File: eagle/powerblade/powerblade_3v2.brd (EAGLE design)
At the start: 25.4 x 25.4 mm, 80 parts, among them J1 JTAG_14PIN_IDC-ND, J2 AC_INF3, J4 TC2030-JLINK-NL, Q1 NTS4173, Q4 2SK1829, U1 TPS62122, U2 MCP6V3, U3 MSP430FR5738, U4 NRF51822QF, U6 MAX9910, U7 OPA2369, X1 16MHz, X3 32.768kHz, Y1 UREACH_XTEND

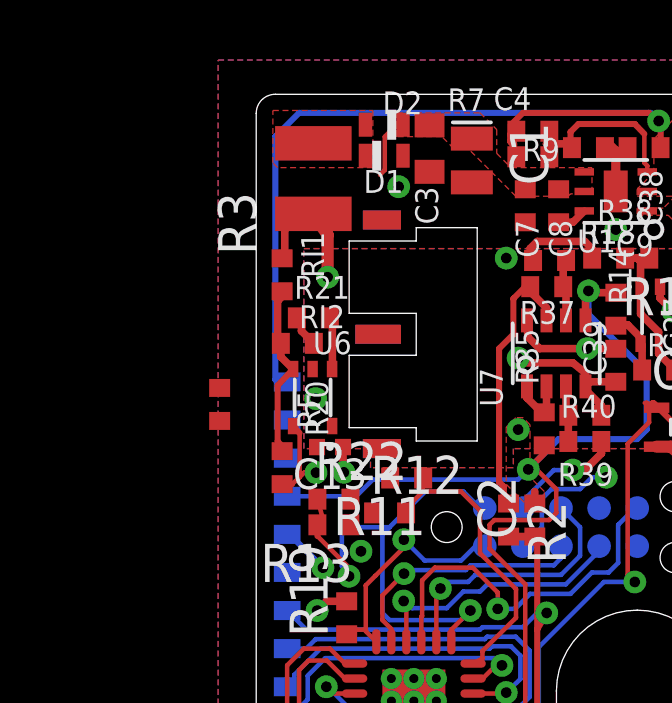
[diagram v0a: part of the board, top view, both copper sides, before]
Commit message: disconnected all but A.4 in F3
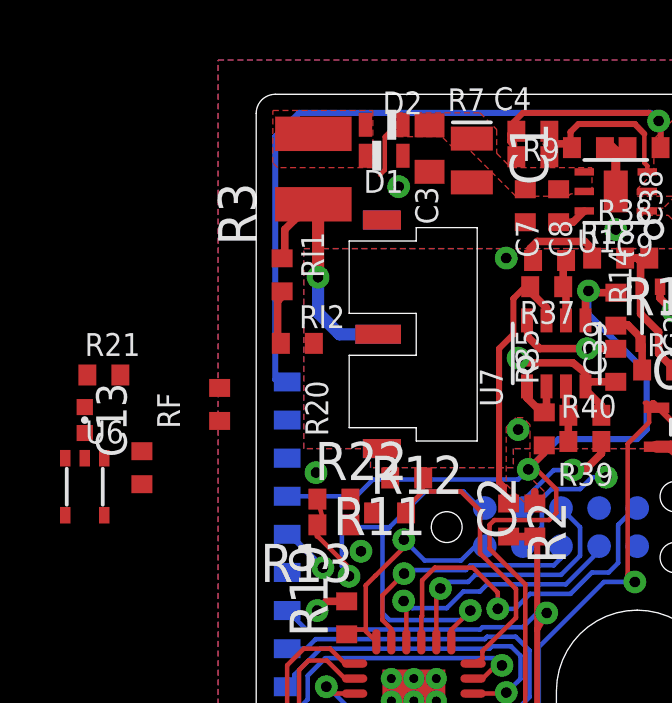
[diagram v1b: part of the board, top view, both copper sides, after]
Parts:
- moved C13 8.23 mm to (-18.4, -2.86), turned to 270 degrees
- moved U6 8.16 mm to (-18.4, -5.08)
- moved R21 7.24 mm to (-17.8, -1.36)
- moved RF 4.67 mm to (-16.5, -4.45)
- moved R3 0.32 mm to (-10.8, 5.51)
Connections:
- net VTEST: no longer J2.PA.1, J2.PA.2, J2.PA.3, J2.PA.5, J2.PA.6
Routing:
- net N$41: track 5.87 -> 1.84 mm
- net VTEST: track 4.37 -> 8.25 mm
- net V_SENSE: track 26.6 -> 23.5 mm
- net N$40: track 1.75 -> 0.00 mm
- net GND3: track 11.5 -> 10.4 mm, vias 7 -> 6
- net +3V3: track 19.3 -> 18.5 mm, vias 10 -> 9

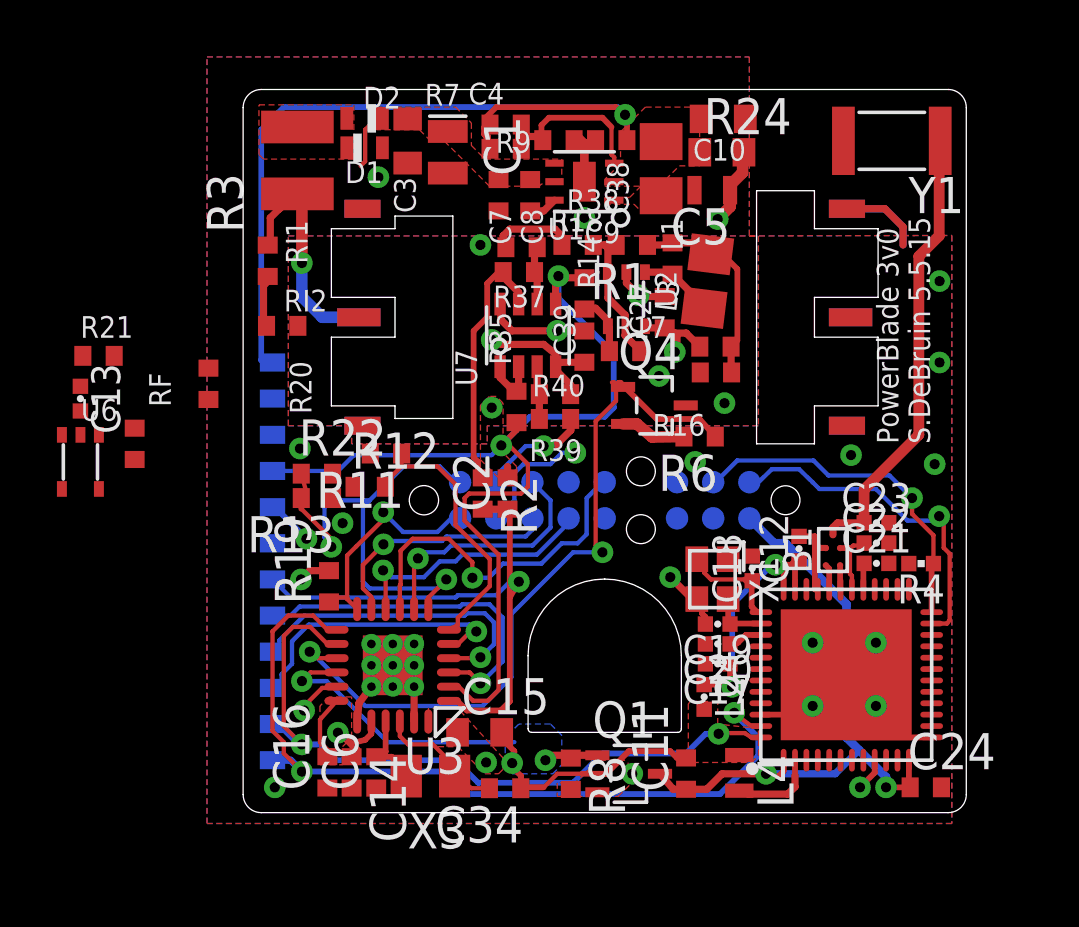
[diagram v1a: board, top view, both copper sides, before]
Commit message: more routing on powerblade and moved Phase contact to top (position 3)
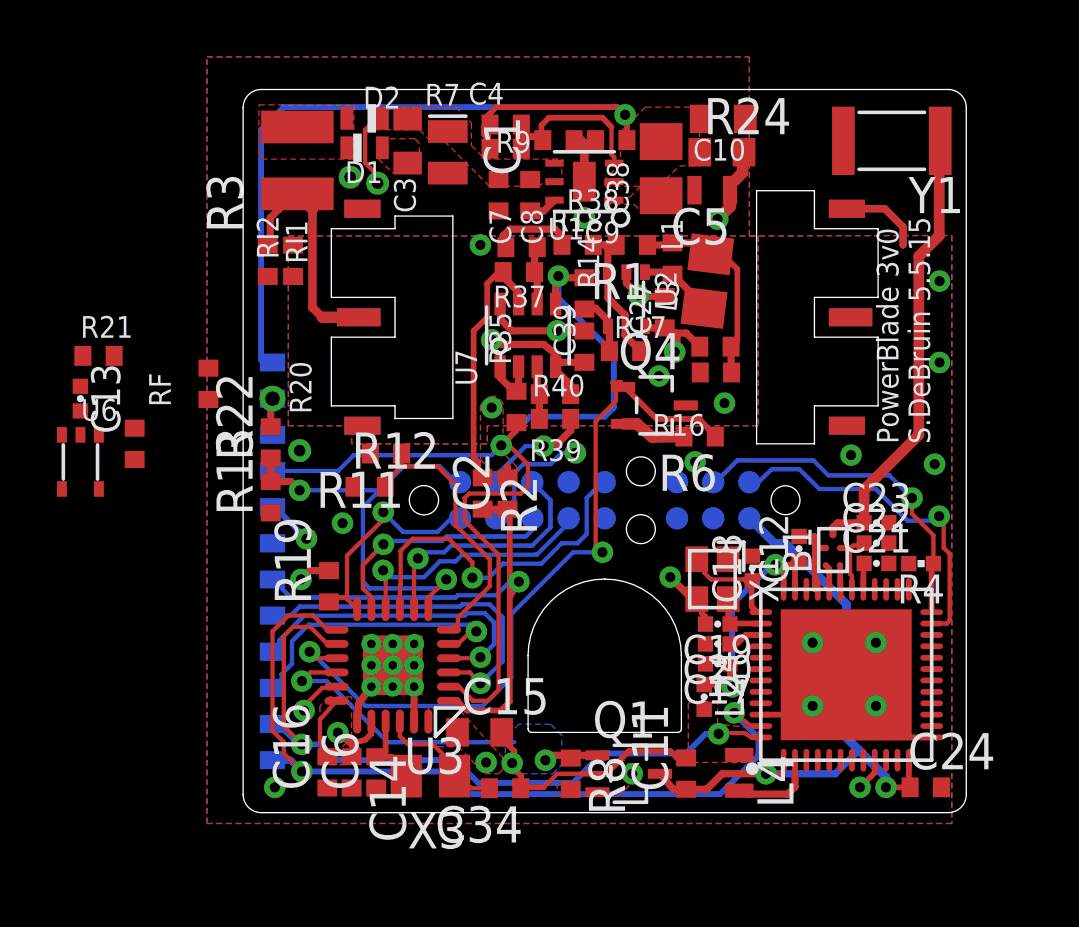
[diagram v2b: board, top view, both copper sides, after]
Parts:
- moved RI2 2.32 mm to (-10.9, 1.98), turned to 270 degrees
- moved R22 1.96 mm to (-11.7, -4.39), turned to 90 degrees
- moved R13 1.62 mm to (-11.7, -6.32), turned to 90 degrees
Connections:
- net VTEST: now also J2.PA.3; no longer J2.PA.4
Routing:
- net V_SENSE: track 23.5 -> 10.2 mm, vias 2 -> 1
- net N$41: track 1.84 -> 0.00 mm
- net TDO: track 17.7 -> 16.1 mm
- net VCC: track 2.38 -> 3.10 mm, vias 0 -> 2
- net ZC: track 0.66 -> 1.01 mm, vias 0 -> 2
- net VTEST: vias 1 -> 0
- net GND: vias 16 -> 15

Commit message: switched pins for vfilt and isense
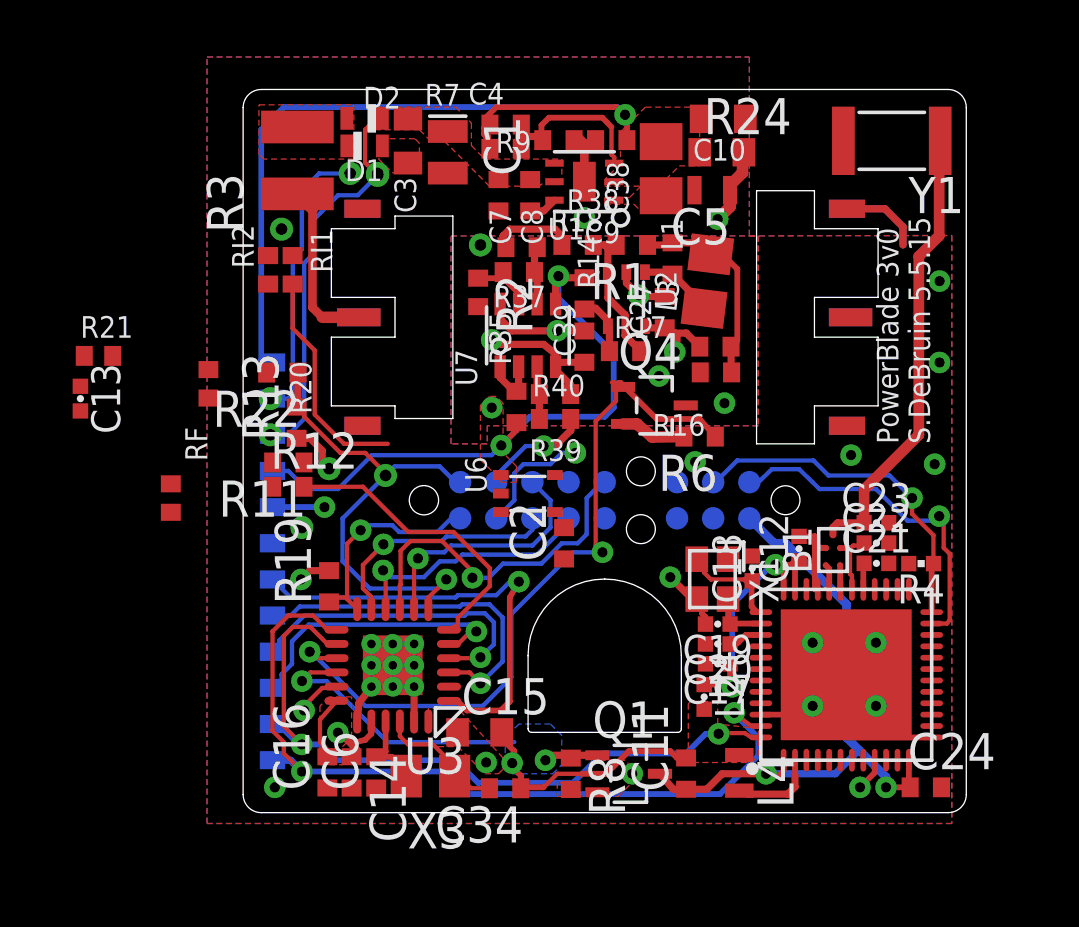
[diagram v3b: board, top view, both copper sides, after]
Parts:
- R2, R20, R21, RF, RI1, RI2: device rcl:R0402_SM -> rcl:R0402
- moved U6 15.8 mm to (-2.70, -6.19), turned to 0 degrees
- moved R2 7.07 mm to (-4.45, 0.87)
- moved R11 3.44 mm to (-11.1, -5.10)
- moved R12 2.86 mm to (-11.1, -5.95)
- moved R13 2.77 mm to (-10.8, -3.70)
- moved C2 2.64 mm to (-1.43, -7.94)
- moved R22 2.49 mm to (-11.3, -1.94), turned to 180 degrees
- moved RF 2.29 mm to (-15.2, -6.35)
- moved RI1 0.93 mm to (-11.0, 1.67)
- moved RI2 0.93 mm to (-11.8, 1.67)
- moved D1 0.07 mm to (-8.43, 6.02)
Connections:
- net GND: now also C2.2
- net GND3: no longer C2.2
- net I_SENSE: now also U3.P2; no longer U3.P1
- net VFILT: now also U3.P1; no longer U3.P2
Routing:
- net VFILT: track 35.0 -> 21.9 mm
- net VCC: track 3.10 -> 14.2 mm
- net ZC: track 1.01 -> 10.0 mm, vias 2 -> 1
- net GND3: track 10.4 -> 19.0 mm, vias 6 -> 7
- net N$41: track 0.00 -> 7.90 mm
- net N$1: track 9.61 -> 2.48 mm
- net I_SENSE: track 20.0 -> 15.6 mm
- net VTEST: track 8.25 -> 5.98 mm
- net GND: track 41.8 -> 43.6 mm, vias 15 -> 16
- net TDO: track 16.1 -> 17.5 mm
- net VCC_SENSE: track 9.85 -> 10.5 mm

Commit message: more routing in new powerblade
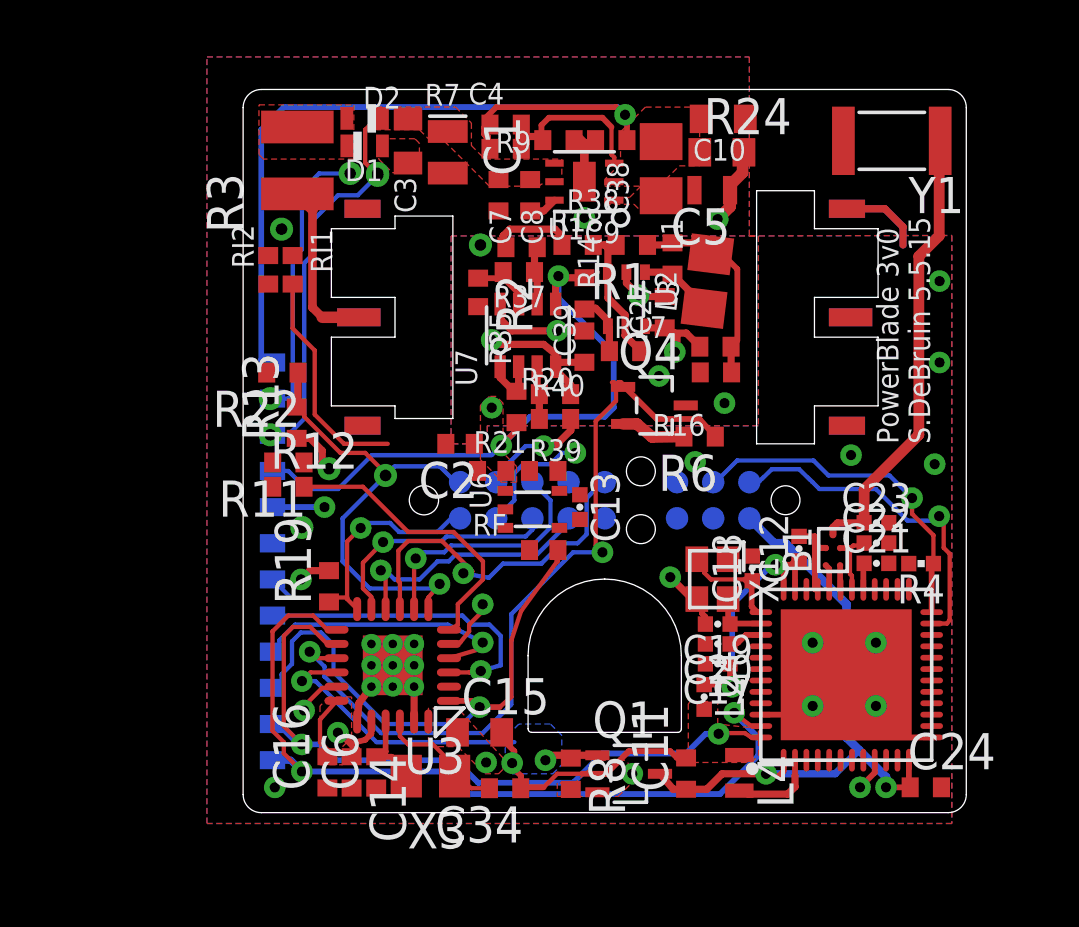
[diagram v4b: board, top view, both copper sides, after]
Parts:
- C2: device rcl:C0402_SM -> rcl:C0402
- moved C13 18.0 mm to (-0.87, -6.67)
- moved R21 14.4 mm to (-3.97, -5.40)
- moved RF 13.2 mm to (-2.14, -8.18), turned to 0 degrees
- moved R20 12.2 mm to (-2.14, -5.40), turned to 0 degrees
- moved C2 5.05 mm to (-5.08, -4.45), turned to 180 degrees
- moved U6 0.58 mm to (-2.54, -6.75)
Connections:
- net I_SENSE: now also U3.P5; no longer U3.P2
- net VFILT: now also U3.P2; no longer U3.P1
- net V_SENSE: now also U3.P1; no longer U3.P5
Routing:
- net I_SENSE: track 15.6 -> 2.96 mm
- net V_SENSE: track 10.2 -> 19.0 mm
- net PWM_VOLTAGE: track 11.2 -> 9.54 mm
- net METER_ENABLE: track 26.8 -> 28.4 mm
- net PWM_CURRENT: track 12.3 -> 11.2 mm
- net TDO: track 17.5 -> 17.0 mm
- net TMS: track 12.2 -> 12.7 mm

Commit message: updated routing in powerblade
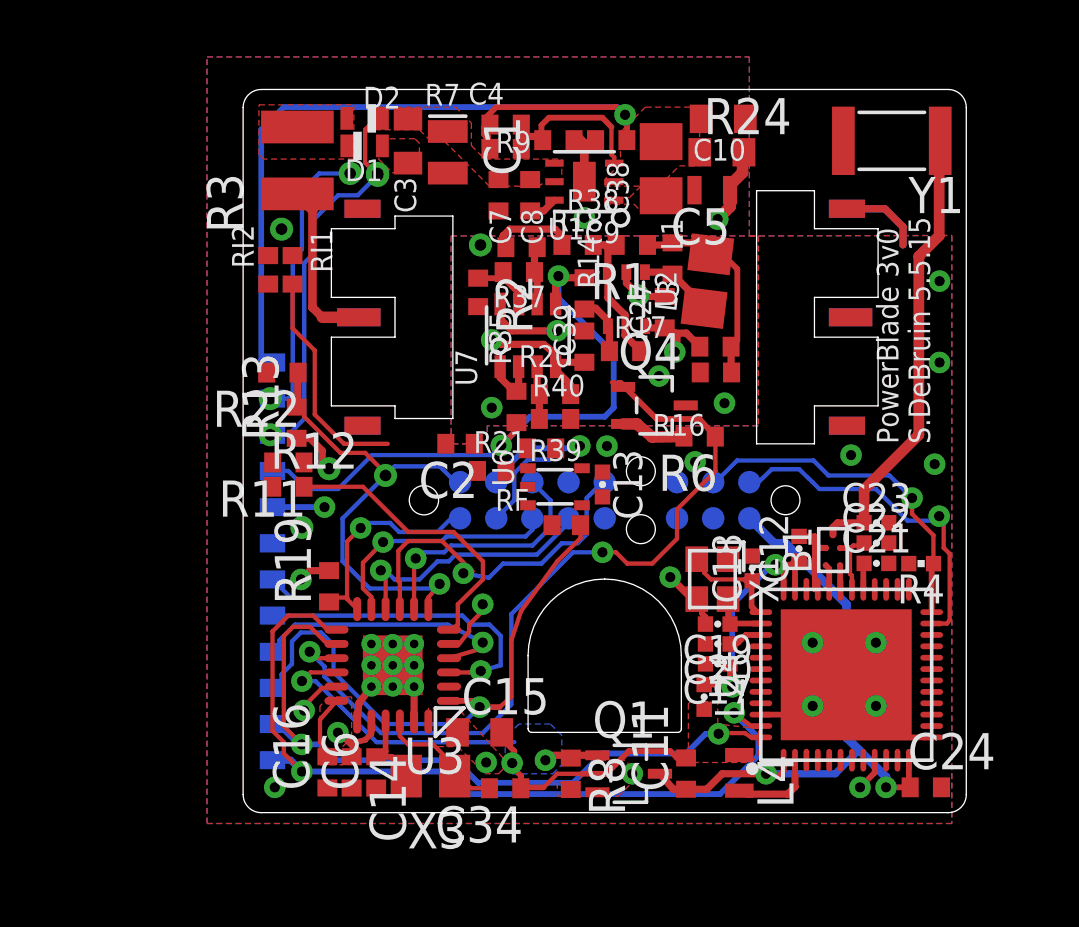
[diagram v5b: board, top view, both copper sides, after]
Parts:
- moved RF 1.18 mm to (-1.35, -7.30)
- moved C13 1.12 mm to (-0.08, -5.87)
- moved U6 1.12 mm to (-1.75, -5.95)
- moved R20 0.80 mm to (-2.22, -4.60)
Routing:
- net V_SENSE: track 19.0 -> 20.2 mm
- net METER_ENABLE: track 28.4 -> 29.5 mm
- net GND: track 43.6 -> 42.6 mm

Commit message: more routing and fixed errors
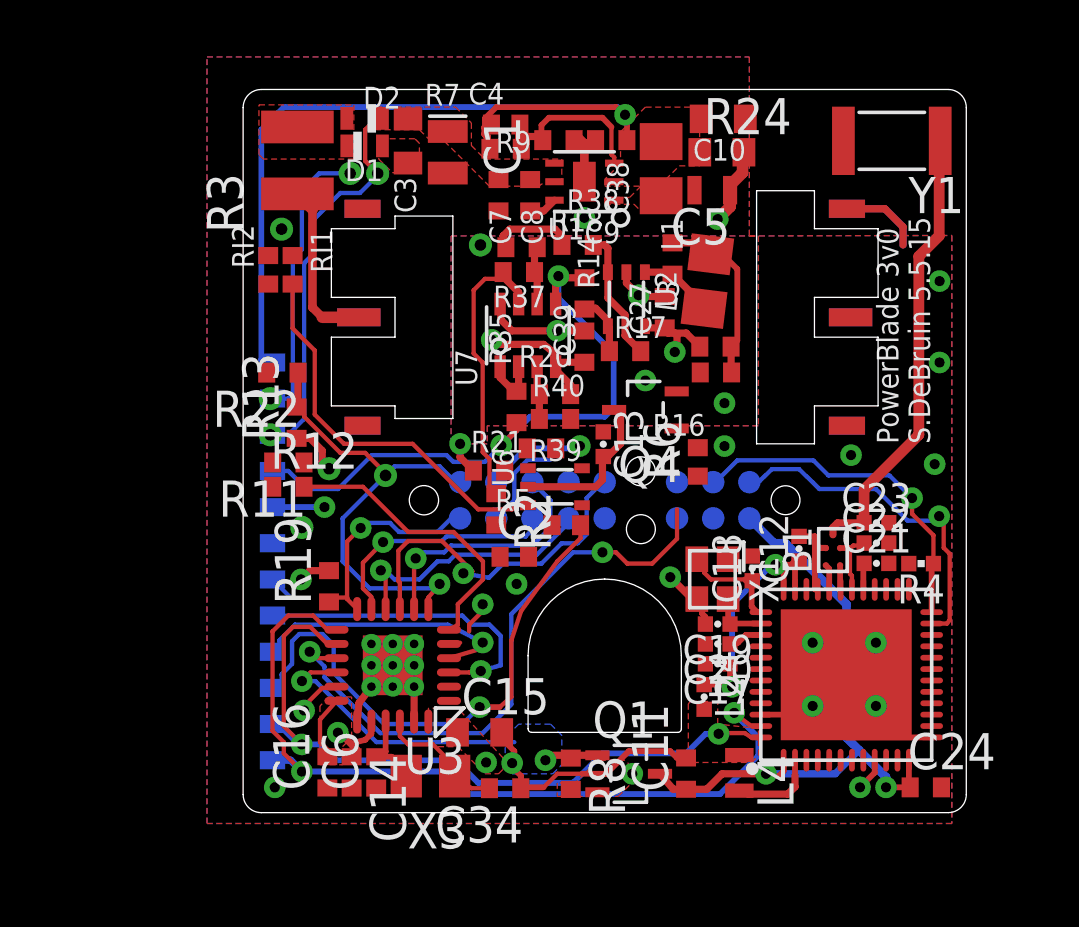
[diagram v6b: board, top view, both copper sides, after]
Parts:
- removed R1: NP, rcl:R0402_SM
- R2, R21: device rcl:R0402 -> rcl:R0402_SM
- R6, R7: device rcl:R0402_SM -> rcl:R0402
- moved R2 7.65 mm to (-3.81, -6.75)
- moved C2 4.40 mm to (-3.17, -8.41), turned to 0 degrees
- moved C13 1.42 mm to (-0.05, -4.46)
- moved R6 0.89 mm to (3.27, -5.08), turned to 90 degrees
- moved Q4 0.35 mm to (1.43, -3.25), turned to 180 degrees
- moved R21 0.10 mm to (-4.06, -5.38)
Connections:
- net N$37: no longer R1.1
- net N$65: no longer R1.2
- net VFILT: no longer U3.P2
- net V_SENSE: now also U3.P2; no longer U3.P1
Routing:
- net METER_ENABLE: track 29.5 -> 21.4 mm
- net N$1: track 2.48 -> 10.3 mm
- net GND3: track 19.0 -> 25.9 mm
- net N$41: track 7.90 -> 13.8 mm
- net GND: track 42.6 -> 40.3 mm
- net V_SENSE: track 20.2 -> 19.2 mm
- net N$37: track 7.30 -> 6.50 mm
- net I_SENSE: track 2.96 -> 2.46 mm
- net VCC: vias 2 -> 1
